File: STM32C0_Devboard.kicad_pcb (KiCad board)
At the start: 2 copper layers, 26 x 40 mm, 14 parts, among them J1 Programming, J2 Left Connector, J3 Right Connector, SW1 SW_Push, U2 STM32C031G6Ux, U3 AZ1117IH-3.3TRE1

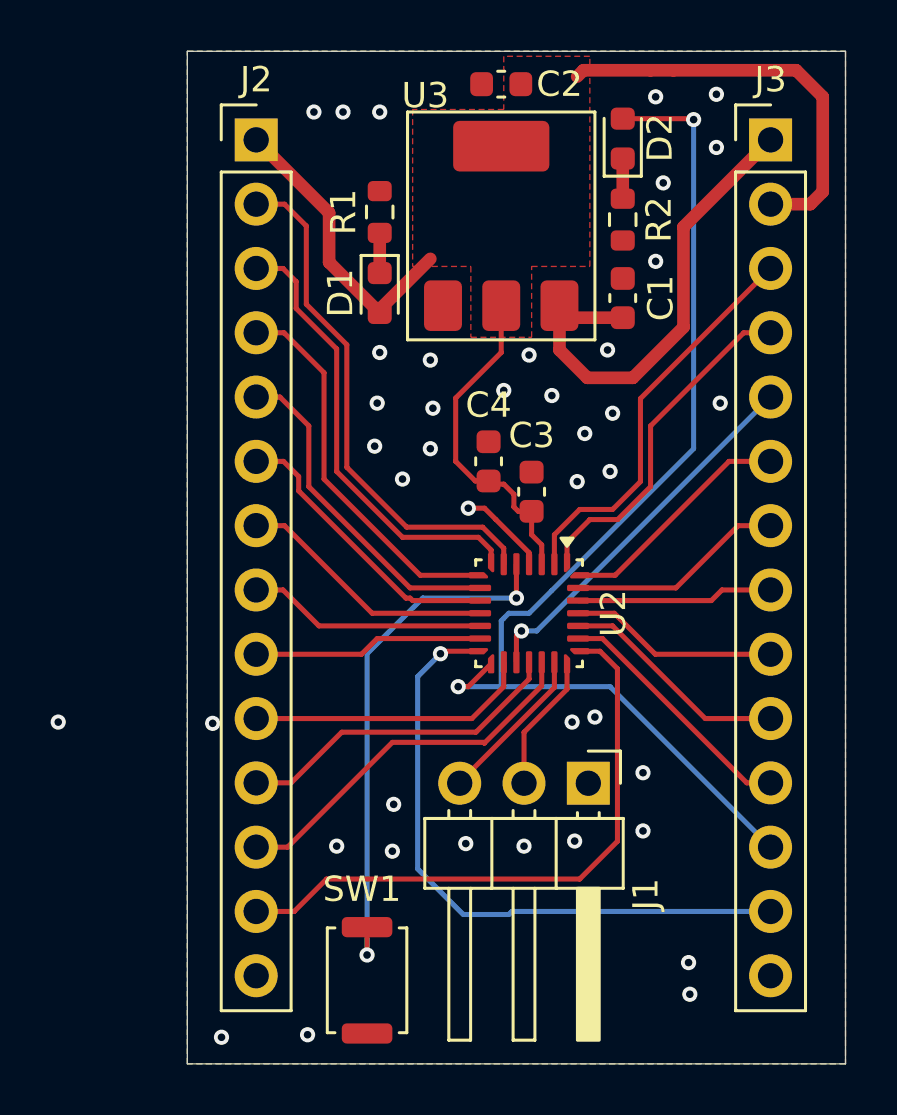
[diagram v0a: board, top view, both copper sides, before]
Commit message: Added Silkscreen, Moved LEDs for clearance
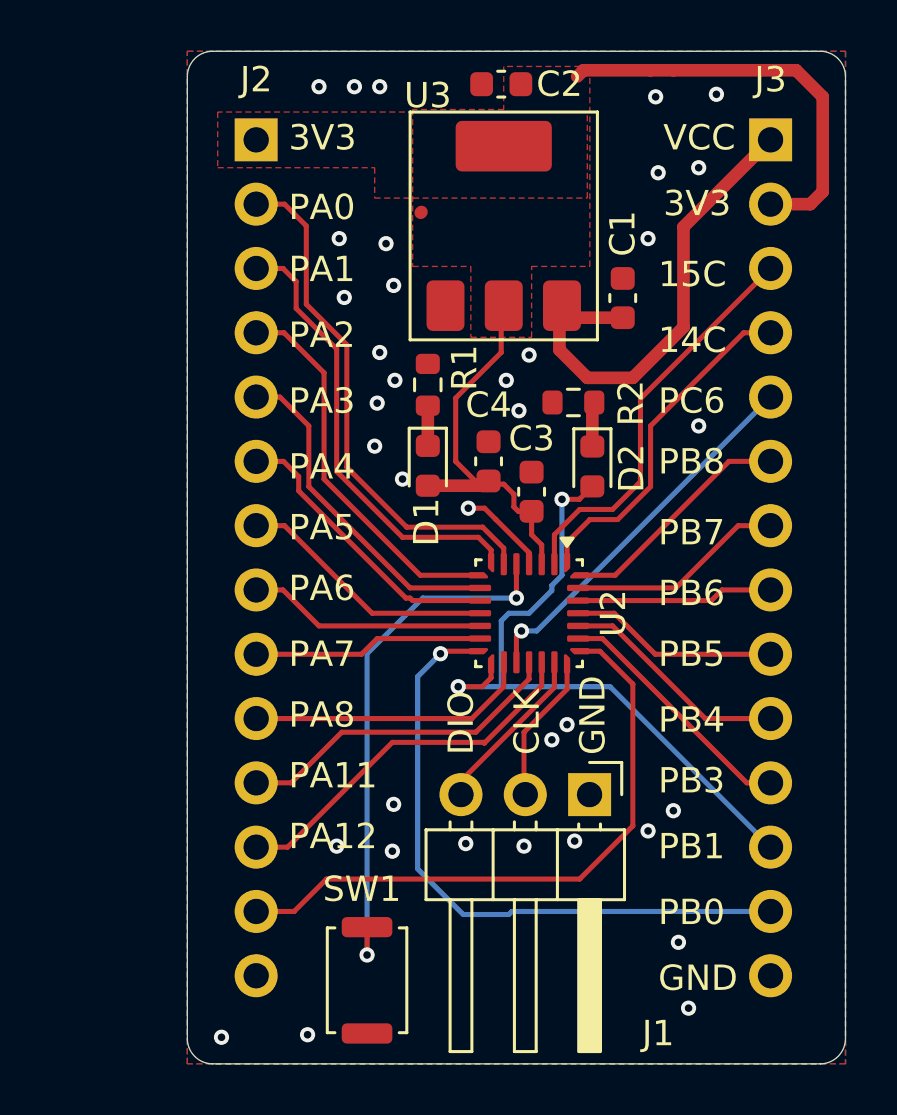
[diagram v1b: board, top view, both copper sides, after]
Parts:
- J2, J3: moved to B.Cu
- moved D2 13.0 mm to (114.0, 81.4), turned to -90 degrees
- moved R2 7.48 mm to (113.2, 78.9), turned to 180 degrees
- moved D1 7.08 mm to (107.5, 81.4)
- moved R1 7.08 mm to (107.5, 78.2)
- moved J1 0.45 mm to (113.9, 94.4)
- moved U3 0.10 mm to (110.5, 71.9)
- turned J2 to 180 degrees
- turned J3 to 180 degrees
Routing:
- net /PB1: track 45.6 -> 27.3 mm
- net +3.3V: track 41.5 -> 32.2 mm
- net /PA15: track 24.7 -> 25.2 mm
- net GND: vias 40 -> 36
- net (no net): vias 1 -> 0
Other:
- outline, holes or cut-outs redrawn
- board text added: "14C"
- board text added: "15C"
- board text added: "3V3"
- board text added: "CLK"
- board text added: "DIO"
- board text added: "GND"
- board text added: "PA0"
- board text added: "PA1"
- board text added: "PA11"
- board text added: "PA12"
- board text added: "PA15"
- board text added: "PA2"
- board text added: "PA3"
- board text added: "PA4"
- board text added: "PA5"
- board text added: "PA6"
- board text added: "PA7"
- board text added: "PA8"
- board text added: "PB0"
- board text added: "PB1"
- board text added: "PB3"
- board text added: "PB4"
- board text added: "PB5"
- board text added: "PB6"
- board text added: "PB7"
- board text added: "PB8"
- board text added: "PC14"
- board text added: "PC15"
- board text added: "PC6"
- board text added: "STM32C031 Dev Board Cody Grandy, 2026 V1.0"
- board text added: "VCC"
